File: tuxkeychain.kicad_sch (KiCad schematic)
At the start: 43 parts, among them J1 Amphenol_10104111, Q2 2N7002, SW1 B3U-1000P, U4 F1C100s, U5 TLV76701DRVx, U6 W25Q128JVS, U7 TLV76701DRVx, U8 TLV76701DRVx, Y1 24MHz

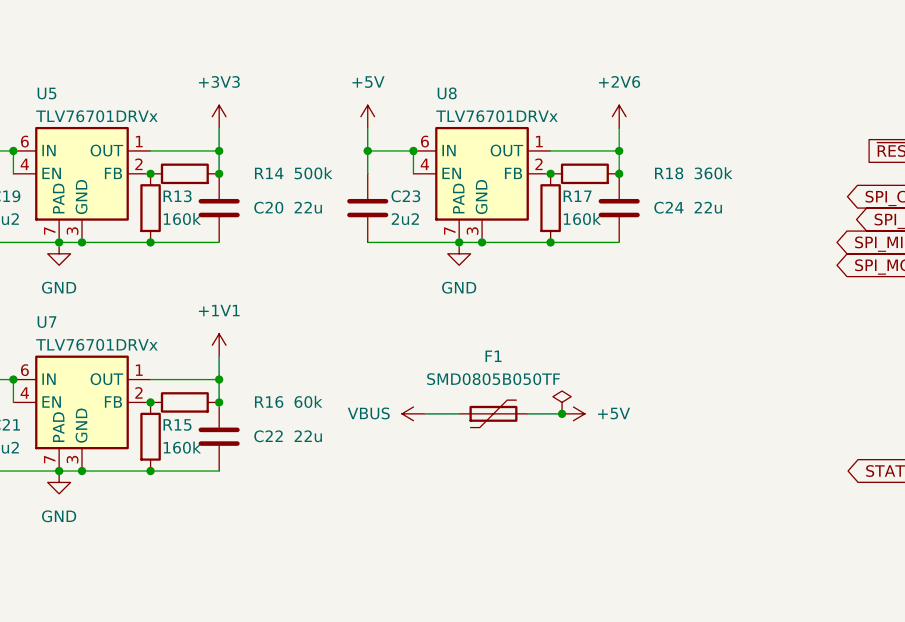
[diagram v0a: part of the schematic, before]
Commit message: Update resistor values in schematic to standard E12 values
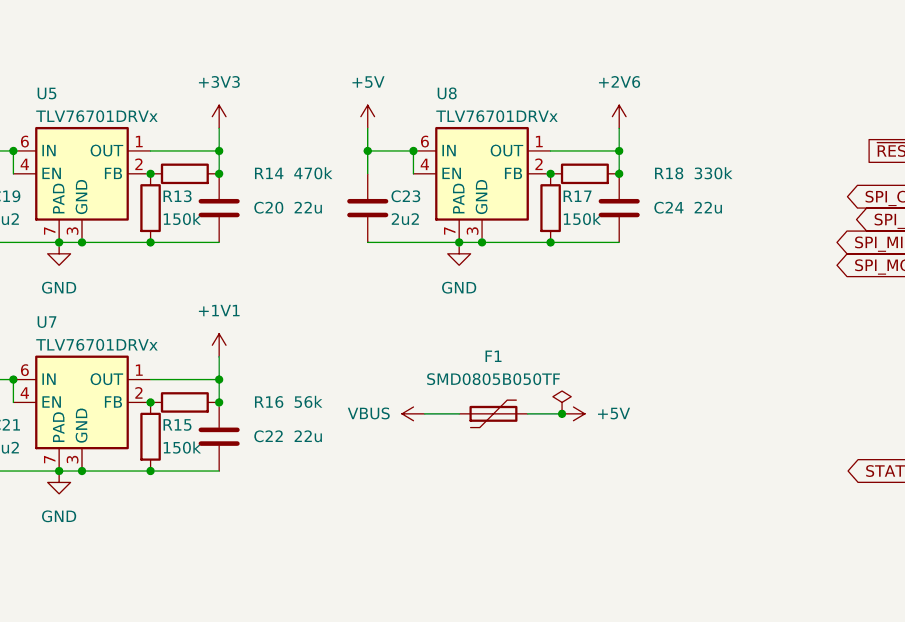
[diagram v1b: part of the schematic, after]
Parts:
- R13, R15, R17: value 160k -> 150k
- R14: value 500k -> 470k
- R16: value 60k -> 56k
- R18: value 360k -> 330k
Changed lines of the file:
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@@
 			)
 		)
-		(property "Value" "160k"
+		(property "Value" "150k"
 			(at 54.61 36.83 0)
 			(effects
@@
 			)
 		)
-		(property "Value" "500k"
+		(property "Value" "470k"
 			(at 69.215 31.75 90)
 			(effects
@@
 			)
 		)
-		(property "Value" "160k"
+		(property "Value" "150k"
 			(at 54.61 62.23 0)
 			(effects
@@
 			)
 		)
-		(property "Value" "60k"
+		(property "Value" "56k"
 			(at 69.215 57.15 90)
 			(effects
@@
 			)
 		)
-		(property "Value" "160k"
+		(property "Value" "150k"
 			(at 99.06 36.83 0)
 			(effects
@@
 			)
 		)
-		(property "Value" "360k"
+		(property "Value" "330k"
 			(at 113.665 31.75 90)
 			(effects

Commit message: rev 2
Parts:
- added J2: FFC 24P 0.5mm, Connector_FFC-FPC:Jushuo_AFC07-S24FCA-00_1x24-1MP_P0.50_Horizontal, symbol Connector_Generic_MountingPin:Conn_01x24_MountingPin
- C20, C22, C24, R13, R14, R15, R16, R17, R18: footprint (none) -> Resistor_SMD:R_0603_1608Metric
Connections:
- net +1V1: now also J2.21 (Pin_21)
- net +2V6: now also J2.22 (Pin_22)
- net +3V3: now also J2.23 (Pin_23)
- net +5V: now also J2.24 (Pin_24)
- net GND: now also J2.MP (MountPin)
- net JTAG_TCK: now also J2.17 (Pin_17)
- net JTAG_TDI: now also J2.19 (Pin_19)
- net JTAG_TDO: now also J2.18 (Pin_18)
- net JTAG_TMS: now also J2.20 (Pin_20)
- net SCL: now also J2.14 (Pin_14)
- net SDA: now also J2.13 (Pin_13)
- net UART_RX: now also J2.16 (Pin_16)
- net UART_TX: now also J2.15 (Pin_15)
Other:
- note removed: "TODO: add a unsoldered SMT header for hacking potential"

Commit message: imrptoravnemtn
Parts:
- J2: value FFC 24P 0.5mm -> expansion
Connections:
- net GND: now also J2.20 (Pin_20); no longer U4.87 (MICIN)
- net SCL: now also J2.13 (Pin_13); no longer J2.14 (Pin_14)
- net SDA: now also J2.12 (Pin_12); no longer J2.13 (Pin_13)
- net UART_RX: now also J2.11 (Pin_11); no longer J2.16 (Pin_16)
- net UART_TX: now also J2.10 (Pin_10); no longer J2.15 (Pin_15)
- net MICIN: now reaches J2.1 (Pin_1)
- net MICIN: now also U4.87 (MICIN)
- net SPI1_MISO: now reaches J2.2 (Pin_2)
- net SPI1_MISO: now also U4.39 (PE10/CSI_D7/UART2_CTS/SPI1_MISO/EINTE10)
- net SPI1_CLK: now reaches J2.3 (Pin_3)
- net SPI1_CLK: now also U4.40 (PE9/CSI_D6/UART2_RTS/SPI1_CLK/EINTE9)
- net SPI1_MOSI: now reaches J2.4 (Pin_4)
- net SPI1_MOSI: now also U4.41 (PE8/CSI_D5/UART2_RX/SPI1_MOSI/EINTE8)
- net SPI1_CS: now reaches J2.5 (Pin_5)
- net SPI1_CS: now also U4.42 (PE7/CSI_D4/UART2_TX/SPI1_CS/EINTE7)
- net HPCOM: now reaches J2.6 (Pin_6)
- net HPCOM: now also U4.3 (HPCOM)
- net HPL: now reaches J2.7 (Pin_7)
- net HPL: now also U4.1 (HPL)
- net HPR: now reaches J2.8 (Pin_8)
- net HPR: now also U4.88 (HPR)
- net TVOUT: now reaches J2.9 (Pin_9)
- net TVOUT: now also U4.72 (TVOUT)
- net SDC0_D3: now reaches U4.54 (PF4/SDC0_D3/UART0_TX/EINTF4)
- net SDC0_D3: now also J2.15 (Pin_15)
- net SDC0_CLK: now reaches U4.56 (PF2/SDC0_CLK/UART0_RX/EINTF2)
- net SDC0_CLK: now also J2.17 (Pin_17)
- net JTAG_TCK renamed SDC0_D2/JTAG_TCK
- net SDC0_D2/JTAG_TCK: now also J2.14 (Pin_14); no longer J2.17 (Pin_17)
- net JTAG_TDI renamed SDC0_D0/JTAG_TDI
- net SDC0_D0/JTAG_TDI: now also J2.18 (Pin_18); no longer J2.19 (Pin_19)
- net JTAG_TDO renamed SDC0_CMD/JTAG_TDO
- net SDC0_CMD/JTAG_TDO: now also J2.16 (Pin_16); no longer J2.18 (Pin_18)
- net JTAG_TMS renamed SDC0_D1/JTAG_TMS
- net SDC0_D1/JTAG_TMS: now also J2.19 (Pin_19); no longer J2.20 (Pin_20)
- no-connect marks 44 -> 30
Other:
- note removed: "in the original schematic all gnd symbols faced down except these"
- note removed: "maybe they are cursed, or maybe the designer was lazy. TODO: exorcism"
- moved on the sheet: J2

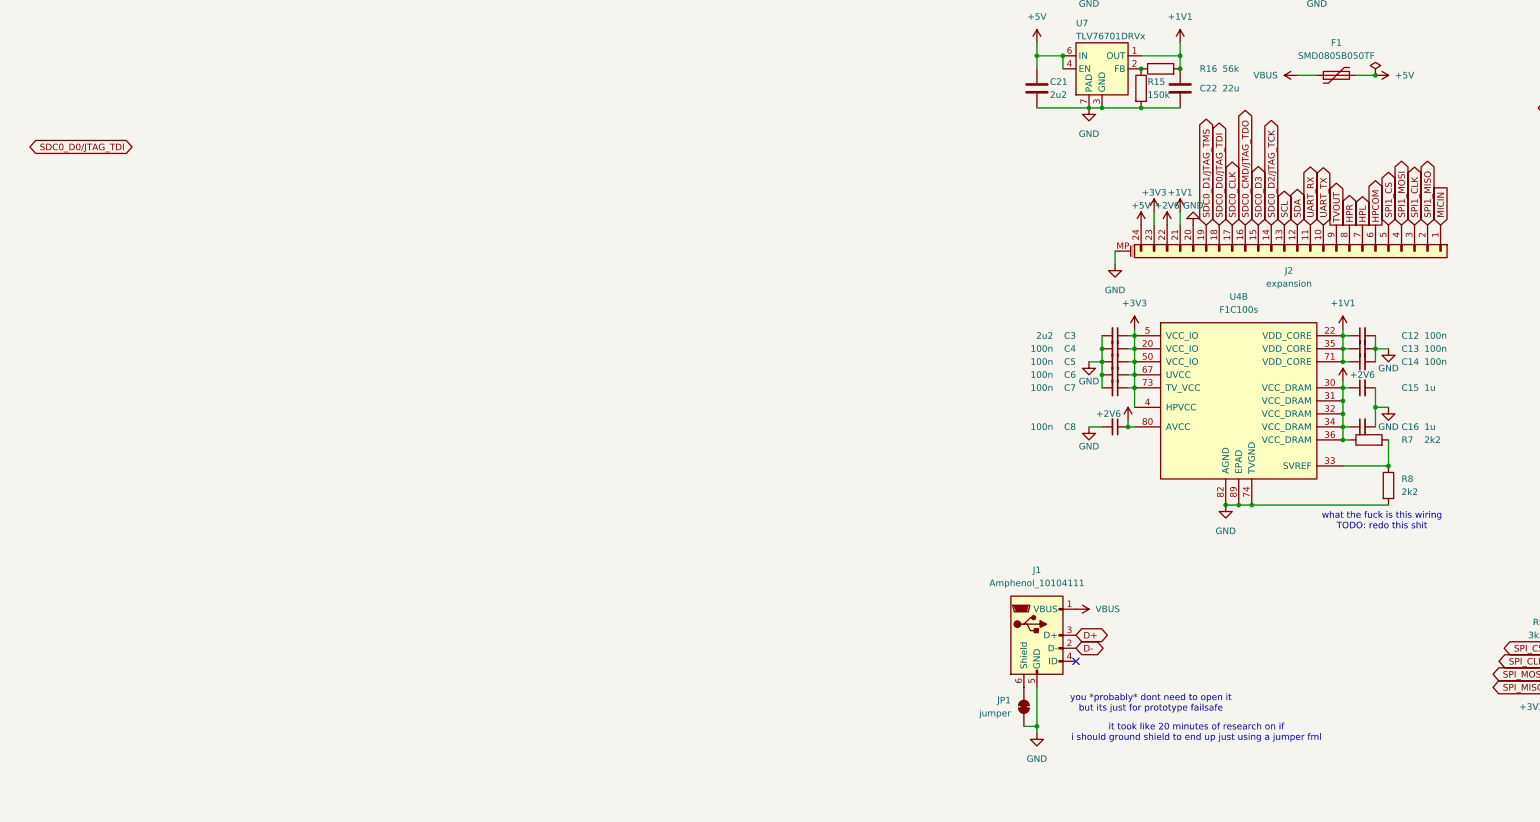
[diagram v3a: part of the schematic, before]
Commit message: Added expansion connectors to schematic
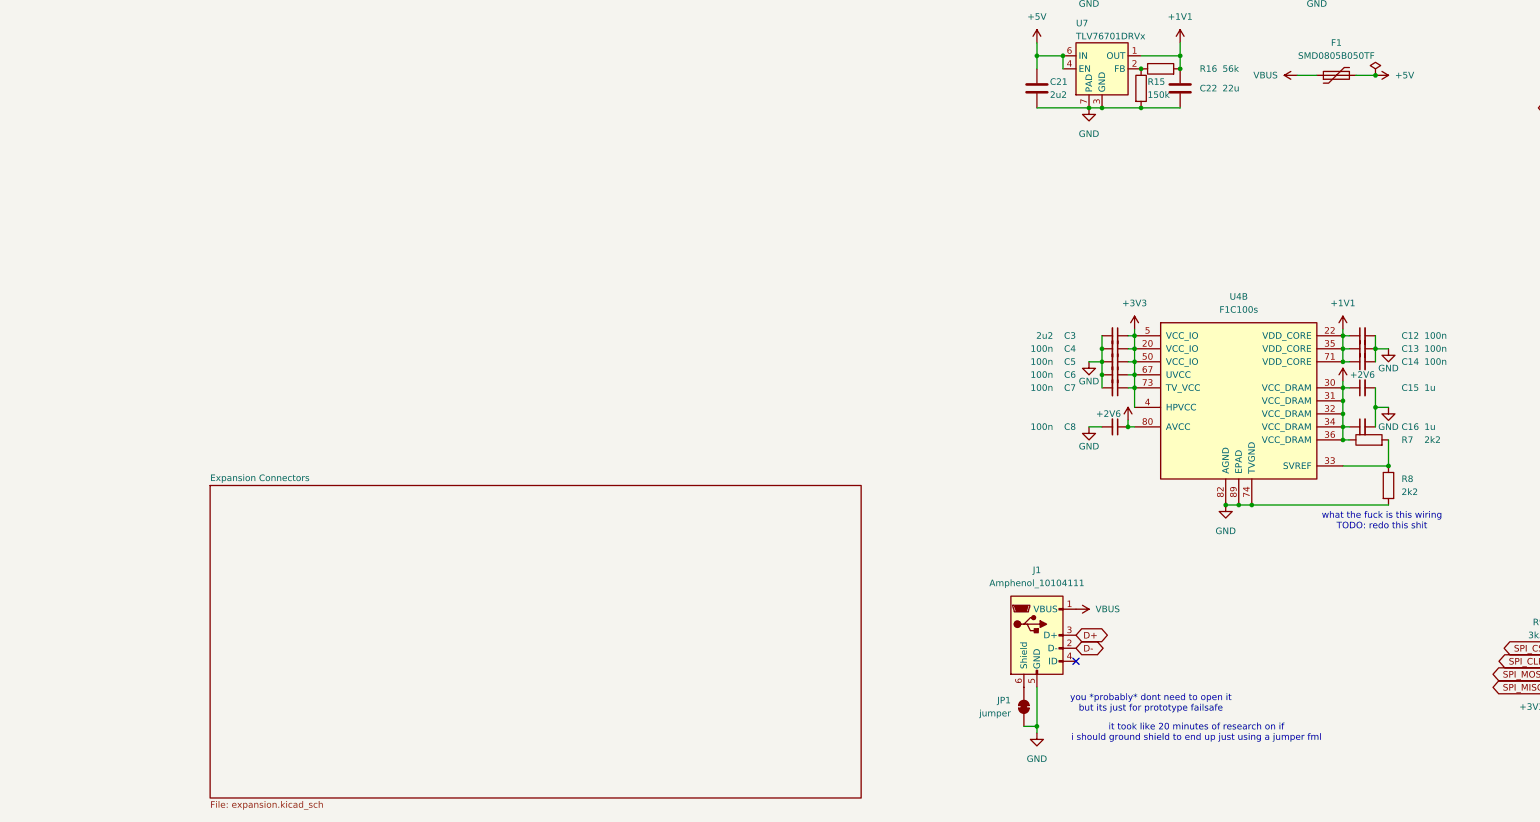
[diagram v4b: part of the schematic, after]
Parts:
- removed J2: expansion, Connector_FFC-FPC:Jushuo_AFC07-S24FCA-00_1x24-1MP_P0.50_Horizontal, symbol Connector_Generic_MountingPin:Conn_01x24_MountingPin
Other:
- added sheet Expansion Connectors (expansion.kicad_sch)

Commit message: work
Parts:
- C12, C13, C14, C15, C16, C17, C18, C19, C21, C23, C3, C4, C5, C6, C7, C8: footprint Capacitor_SMD:C_0603_1608Metric -> Capacitor_SMD:C_0402_1005Metric
- C20, C22, C24: footprint Resistor_SMD:R_0603_1608Metric -> Capacitor_SMD:C_0402_1005Metric
- R10, R11, R12, R13, R14, R15, R16, R17, R18, R7, R8, R9: footprint Resistor_SMD:R_0603_1608Metric -> Resistor_SMD:R_0402_1005Metric
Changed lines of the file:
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@@
 			)
 		)
-		(property "Footprint" "Capacitor_SMD:C_0603_1608Metric"
+		(property "Footprint" "Capacitor_SMD:C_0402_1005Metric"
 			(at 274.32 32.7152 0)
 			(effects
@@
 			)
 		)
-		(property "Footprint" "Resistor_SMD:R_0603_1608Metric"
+		(property "Footprint" "Resistor_SMD:R_0402_1005Metric"
 			(at 51.562 35.56 90)
 			(effects
@@
 			)
 		)
-		(property "Footprint" "Capacitor_SMD:C_0603_1608Metric"
+		(property "Footprint" "Capacitor_SMD:C_0402_1005Metric"
 			(at 33.9852 64.77 0)
 			(effects
@@
 			)
 		)
-		(property "Footprint" "Capacitor_SMD:C_0603_1608Metric"
+		(property "Footprint" "Capacitor_SMD:C_0402_1005Metric"
 			(at 274.32 23.1648 0)
 			(effects
@@
 			)
 		)
-		(property "Footprint" "Resistor_SMD:R_0603_1608Metric"
+		(property "Footprint" "Capacitor_SMD:C_0402_1005Metric"
 			(at 61.9252 64.77 0)
 			(effects
@@
 			)
 		)
-		(property "Footprint" "Resistor_SMD:R_0603_1608Metric"
+		(property "Footprint" "Resistor_SMD:R_0402_1005Metric"
 			(at 99.822 138.43 90)
 			(effects
@@
 			)
 		)
-		(property "Footprint" "Resistor_SMD:R_0603_1608Metric"
+		(property "Footprint" "Resistor_SMD:R_0402_1005Metric"
 			(at 57.15 33.528 90)
 			(effects
@@
 			)
 		)
-		(property "Footprint" "Capacitor_SMD:C_0603_1608Metric"
+		(property "Footprint" "Capacitor_SMD:C_0402_1005Metric"
 			(at 78.4352 39.37 0)
 			(effects
@@
 			)
 		)
-		(property "Footprint" "Resistor_SMD:R_0603_1608Metric"
+		(property "Footprint" "Capacitor_SMD:C_0402_1005Metric"
 			(at 61.9252 39.37 0)
 			(effects
@@
 			)
 		)
-		(property "Footprint" "Capacitor_SMD:C_0603_1608Metric"
+		(property "Footprint" "Capacitor_SMD:C_0402_1005Metric"
 			(at 96.52 114.3 0)
 			(effects
@@
 			)
 		)
-		(property "Footprint" "Capacitor_SMD:C_0603_1608Metric"
+		(property "Footprint" "Capacitor_SMD:C_0402_1005Metric"
 			(at 96.52 111.76 0)
 			(effects
@@
 			)
 		)
-		(property "Footprint" "Resistor_SMD:R_0603_1608Metric"
+		(property "Footprint" "Resistor_SMD:R_0402_1005Metric"
 			(at 225.298 142.24 90)
 			(effects
@@
 			)
 		)
-		(property "Footprint" "Capacitor_SMD:C_0603_1608Metric"
+		(property "Footprint" "Capacitor_SMD:C_0402_1005Metric"
 			(at 48.26 111.76 0)
 			(effects
@@
 			)
 		)
-		(property "Footprint" "Capacitor_SMD:C_0603_1608Metric"
+		(property "Footprint" "Capacitor_SMD:C_0402_1005Metric"
 			(at 48.26 116.84 0)
 			(effects
@@
 			)
 		)
-		(property "Footprint" "Capacitor_SMD:C_0603_1608Metric"
+		(property "Footprint" "Capacitor_SMD:C_0402_1005Metric"
 			(at 48.26 109.22 0)
 			(effects
@@
 			)
 		)
-		(property "Footprint" "Resistor_SMD:R_0603_1608Metric"
+		(property "Footprint" "Resistor_SMD:R_0402_1005Metric"
 			(at 132.842 166.37 90)
 			(effects
@@
 			)
 		)
-		(property "Footprint" "Resistor_SMD:R_0603_1608Metric"
+		(property "Footprint" "Resistor_SMD:R_0402_1005Metric"
 			(at 203.708 142.24 90)
 			(effects
@@
 			)
 		)
-		(property "Footprint" "Resistor_SMD:R_0603_1608Metric"
+		(property "Footprint" "Resistor_SMD:R_0402_1005Metric"
 			(at 97.79 131.318 90)
 			(effects
@@
 			)
 		)
-		(property "Footprint" "Resistor_SMD:R_0603_1608Metric"
+		(property "Footprint" "Capacitor_SMD:C_0402_1005Metric"
 			(at 106.3752 39.37 0)
 			(effects
@@
 			)
 		)
-		(property "Footprint" "Capacitor_SMD:C_0603_1608Metric"
+		(property "Footprint" "Capacitor_SMD:C_0402_1005Metric"
 			(at 48.26 127 0)
 			(effects
@@
 			)
 		)
-		(property "Footprint" "Capacitor_SMD:C_0603_1608Metric"
+		(property "Footprint" "Capacitor_SMD:C_0402_1005Metric"
 			(at 96.52 109.22 0)
 			(effects
@@
 			)
 		)
-		(property "Footprint" "Capacitor_SMD:C_0603_1608Metric"
+		(property "Footprint" "Capacitor_SMD:C_0402_1005Metric"
 			(at 48.26 119.38 0)
 			(effects
@@
 			)
 		)
-		(property "Footprint" "Resistor_SMD:R_0603_1608Metric"
+		(property "Footprint" "Resistor_SMD:R_0402_1005Metric"
 			(at 51.562 60.96 90)
 			(effects
@@
 			)
 		)
-		(property "Footprint" "Resistor_SMD:R_0603_1608Metric"
+		(property "Footprint" "Resistor_SMD:R_0402_1005Metric"
 			(at 57.15 58.928 90)
 			(effects
@@
 			)
 		)
-		(property "Footprint" "Capacitor_SMD:C_0603_1608Metric"
+		(property "Footprint" "Capacitor_SMD:C_0402_1005Metric"
 			(at 33.9852 39.37 0)
 			(effects
@@
 			)
 		)
-		(property "Footprint" "Resistor_SMD:R_0603_1608Metric"
+		(property "Footprint" "Resistor_SMD:R_0402_1005Metric"
 			(at 184.15 140.208 90)
 			(effects
@@
 			)
 		)
-		(property "Footprint" "Capacitor_SMD:C_0603_1608Metric"
+		(property "Footprint" "Capacitor_SMD:C_0402_1005Metric"
 			(at 48.26 114.3 0)
 			(effects
@@
 			)
 		)
-		(property "Footprint" "Resistor_SMD:R_0603_1608Metric"
+		(property "Footprint" "Resistor_SMD:R_0402_1005Metric"
 			(at 96.012 35.56 90)
 			(effects
@@
 			)
 		)
-		(property "Footprint" "Capacitor_SMD:C_0603_1608Metric"
+		(property "Footprint" "Capacitor_SMD:C_0402_1005Metric"
 			(at 96.52 127 0)
 			(effects
@@
 			)
 		)
-		(property "Footprint" "Capacitor_SMD:C_0603_1608Metric"
+		(property "Footprint" "Capacitor_SMD:C_0402_1005Metric"
 			(at 96.52 119.38 0)
 			(effects
@@
 			)
 		)
-		(property "Footprint" "Resistor_SMD:R_0603_1608Metric"
+		(property "Footprint" "Resistor_SMD:R_0402_1005Metric"
 			(at 101.6 33.528 90)
 			(effects
@@
 	)
 	(sheet
-		(at -128.27 138.43)
-		(size 127 60.96)
+		(at 255.27 142.24)
+		(size 22.86 12.7)
 		(exclude_from_sim no)
 		(in_bom yes)
@@
 		)
 		(property "Sheetname" "Expansion Connectors"
-			(at -128.27 137.7184 0)
+			(at 255.27 141.5284 0)
 			(effects
 				(font
@@
 		)
 		(property "Sheetfile" "expansion.kicad_sch"
-			(at -128.27 199.9746 0)
+			(at 255.27 155.5246 0)
 			(effects
 				(font

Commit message: h
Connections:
- no-connect marks 30 -> 34
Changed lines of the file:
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@@
+	)
+	(no_connect
+		(at 140.97 95.25)
 	)
 	(no_connect
@@
 	)
 	(no_connect
+		(at 140.97 100.33)
+	)
+	(no_connect
 		(at 140.97 77.47)
 	)
@@
 	)
 	(no_connect
+		(at 140.97 97.79)
+	)
+	(no_connect
 		(at 140.97 67.31)
 	)
@@
 	)
 	(no_connect
+		(at 140.97 92.71)
+	)
+	(no_connect
